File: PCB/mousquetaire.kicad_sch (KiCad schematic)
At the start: 34 parts, among them J1 Sum2, J2 Sum3, J3 Sum1, J5 SUM, J6 Mi, J7 M1, J8 M2, J9 M3, U1 TL072, U2 TL074

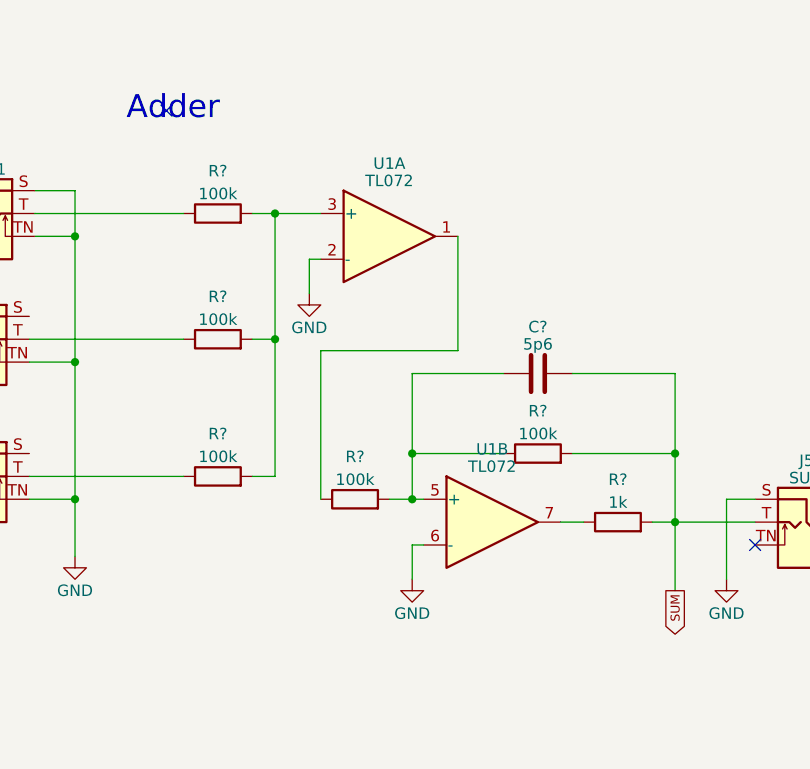
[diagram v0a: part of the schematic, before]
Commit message: :pencil2: Fix the adder circuit
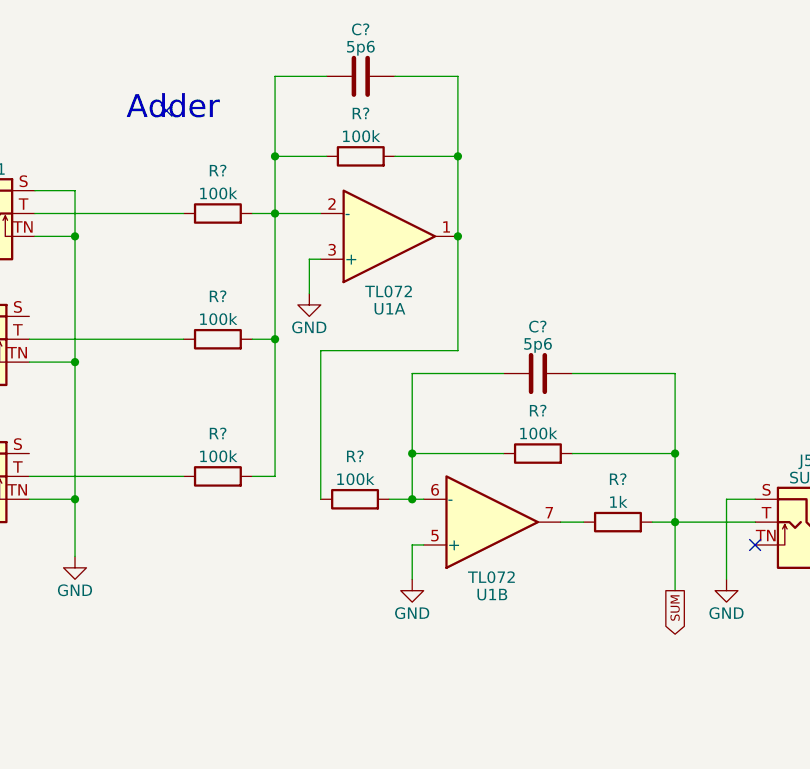
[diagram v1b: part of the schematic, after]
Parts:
- added C?: 5p6, Capacitor_THT:C_Disc_D4.3mm_W1.9mm_P5.00mm, symbol Device:C
- added R?: 100k, Resistor_THT:R_Axial_DIN0207_L6.3mm_D2.5mm_P7.62mm_Horizontal, symbol Device:R
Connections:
- net GND: now also U1.3 (+), U1.5 (+); no longer U1.2 (-), U1.6 (-)
- net at R?.2, R?.2, R?.2: now also U1.2 (-), C?.1, R?.1; no longer U1.3 (+)
- net at R?.1, U1.1: now also C?.2, R?.2
- net at C?.1, R?.1, R?.2: now also U1.6 (-); no longer U1.5 (+)

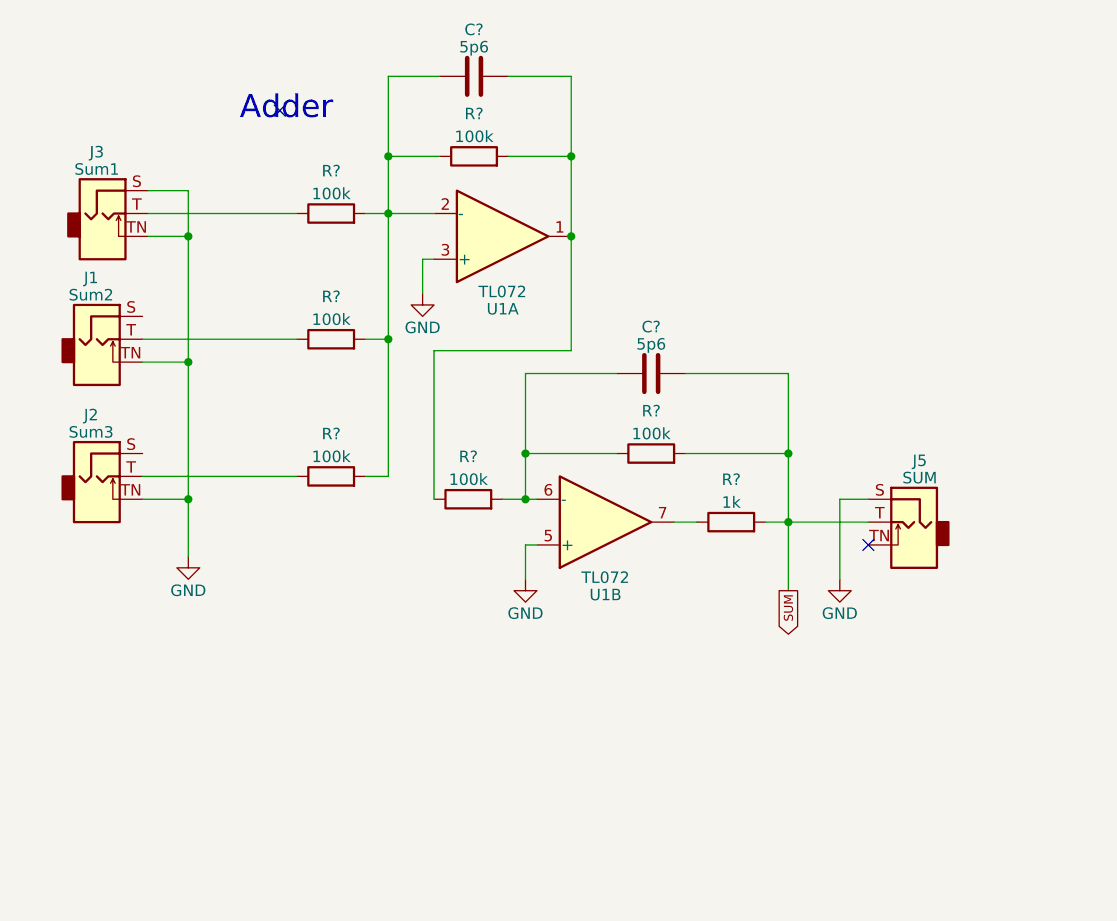
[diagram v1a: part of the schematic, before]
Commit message: :pencil2: Add missing changes for the adder fix
Somehow not everything had been committed for #2. This is the fix. :/
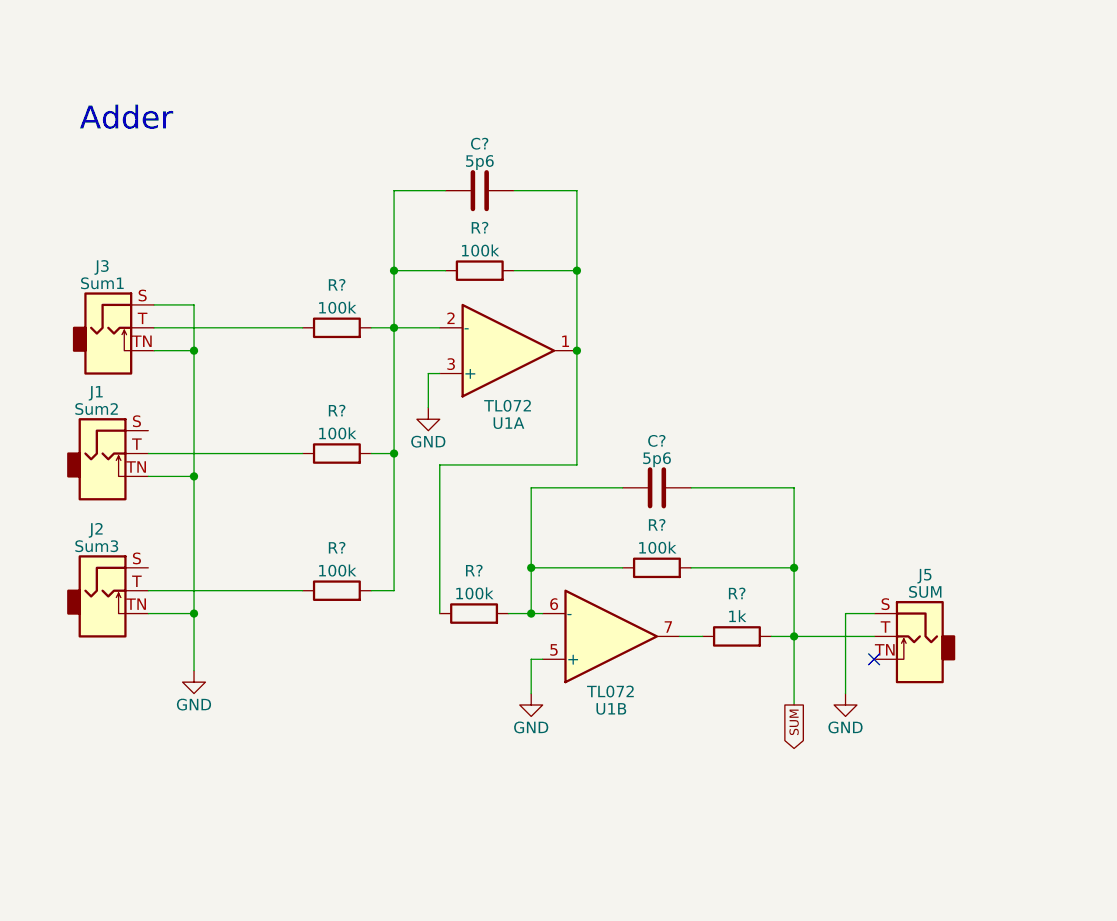
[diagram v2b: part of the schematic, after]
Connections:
- no-connect marks 5 -> 4
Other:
- moved on the sheet: C?, J1, J2, J3, J5, R?, U1A, U1B

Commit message: :art: Improvements to schematic for PCB design
Mostly interchanging components for easier routing.
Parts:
- renumbered R9 to R10, R10 to R11, R7 to R8, R8 to R9
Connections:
- net at U2.6 (-), U2.7: now also R11.1; no longer R10.1
- net at U2.8, U2.9 (-): now also R9.1; no longer R11.1
- net at U2.1, U2.2 (-): now also R10.1; no longer R9.1
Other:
- moved on the sheet: U2A, U2B, U2C
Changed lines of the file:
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@@
       (project "mousquetaire"
         (path "/6467167b-c991-4ed5-b6bb-0d17859f2985"
-          (reference "R11") (unit 1)
+          (reference "R5") (unit 1)
         )
       )
@@
       (project "mousquetaire"
         (path "/6467167b-c991-4ed5-b6bb-0d17859f2985"
-          (reference "C4") (unit 1)
+          (reference "C5") (unit 1)
         )
       )
@@
       (project "mousquetaire"
         (path "/6467167b-c991-4ed5-b6bb-0d17859f2985"
-          (reference "C9") (unit 1)
+          (reference "C10") (unit 1)
         )
       )
@@
       (project "mousquetaire"
         (path "/6467167b-c991-4ed5-b6bb-0d17859f2985"
-          (reference "C7") (unit 1)
+          (reference "C8") (unit 1)
         )
       )
@@
   (symbol (lib_id "Device:R") (at 210.82 60.325 90) (unit 1)
     (in_bom yes) (on_board yes) (dnp no) (fields_autoplaced)
-    (property "Reference" "R9" (at 210.82 55.6092 90)
+    (property "Reference" "R10" (at 210.82 55.6092 90)
       (effects (font (size 1.27 1.27)))
     )
@@
       (project "mousquetaire"
         (path "/6467167b-c991-4ed5-b6bb-0d17859f2985"
-          (reference "R9") (unit 1)
+          (reference "R10") (unit 1)
         )
       )
@@
       (project "mousquetaire"
         (path "/6467167b-c991-4ed5-b6bb-0d17859f2985"
-          (reference "C10") (unit 1)
+          (reference "C3") (unit 1)
         )
       )
@@
     )
   )
-  (symbol (lib_id "Amplifier_Operational:TL074") (at 195.58 60.325 0) (unit 2)
-    (in_bom yes) (on_board yes) (dnp no) (fields_autoplaced)
-    (property "Reference" "U2" (at 195.58 52.2351 0)
-      (effects (font (size 1.27 1.27)))
-    )
-    (property "Value" "TL074" (at 195.58 54.1561 0)
-      (effects (font (size 1.27 1.27)))
-    )
-    (property "Footprint" "Package_DIP:DIP-14_W7.62mm_Socket_LongPads" (at 194.31 57.785 0)
-      (effects (font (size 1.27 1.27)) hide)
-    )
-    (property "Datasheet" "http://www.ti.com/lit/ds/symlink/tl071.pdf" (at 196.85 55.245 0)
+  (symbol (lib_id "Amplifier_Operational:TL074") (at 195.58 78.105 0) (unit 2)
+    (in_bom yes) (on_board yes) (dnp no) (fields_autoplaced)
+    (property "Reference" "U2" (at 195.58 70.0151 0)
+      (effects (font (size 1.27 1.27)))
+    )
+    (property "Value" "TL074" (at 195.58 71.9361 0)
+      (effects (font (size 1.27 1.27)))
+    )
+    (property "Footprint" "Package_DIP:DIP-14_W7.62mm_Socket_LongPads" (at 194.31 75.565 0)
+      (effects (font (size 1.27 1.27)) hide)
+    )
+    (property "Datasheet" "http://www.ti.com/lit/ds/symlink/tl071.pdf" (at 196.85 73.025 0)
       (effects (font (size 1.27 1.27)) hide)
     )
@@
   (symbol (lib_id "Device:R") (at 210.82 78.105 90) (unit 1)
     (in_bom yes) (on_board yes) (dnp no) (fields_autoplaced)
-    (property "Reference" "R10" (at 210.82 73.3892 90)
+    (property "Reference" "R11" (at 210.82 73.3892 90)
       (effects (font (size 1.27 1.27)))
     )
@@
       (project "mousquetaire"
         (path "/6467167b-c991-4ed5-b6bb-0d17859f2985"
-          (reference "R10") (unit 1)
+          (reference "R11") (unit 1)
         )
       )
@@
       (project "mousquetaire"
         (path "/6467167b-c991-4ed5-b6bb-0d17859f2985"
-          (reference "C6") (unit 1)
+          (reference "C7") (unit 1)
         )
       )
@@
       (project "mousquetaire"
         (path "/6467167b-c991-4ed5-b6bb-0d17859f2985"
-          (reference "R6") (unit 1)
-        )
-      )
-    )
-  )
-  (symbol (lib_id "Amplifier_Operational:TL074") (at 194.31 38.735 0) (unit 1)
-    (in_bom yes) (on_board yes) (dnp no) (fields_autoplaced)
-    (property "Reference" "U2" (at 194.31 30.6451 0)
-      (effects (font (size 1.27 1.27)))
-    )
-    (property "Value" "TL074" (at 194.31 32.5661 0)
-      (effects (font (size 1.27 1.27)))
-    )
-    (property "Footprint" "Package_DIP:DIP-14_W7.62mm_Socket_LongPads" (at 193.04 36.195 0)
-      (effects (font (size 1.27 1.27)) hide)
-    )
-    (property "Datasheet" "http://www.ti.com/lit/ds/symlink/tl071.pdf" (at 195.58 33.655 0)
+          (reference "R7") (unit 1)
+        )
+      )
+    )
+  )
+  (symbol (lib_id "Amplifier_Operational:TL074") (at 195.58 60.325 0) (unit 1)
+    (in_bom yes) (on_board yes) (dnp no) (fields_autoplaced)
+    (property "Reference" "U2" (at 195.58 52.2351 0)
+      (effects (font (size 1.27 1.27)))
+    )
+    (property "Value" "TL074" (at 195.58 54.1561 0)
+      (effects (font (size 1.27 1.27)))
+    )
+    (property "Footprint" "Package_DIP:DIP-14_W7.62mm_Socket_LongPads" (at 194.31 57.785 0)
+      (effects (font (size 1.27 1.27)) hide)
+    )
+    (property "Datasheet" "http://www.ti.com/lit/ds/symlink/tl071.pdf" (at 196.85 55.245 0)
       (effects (font (size 1.27 1.27)) hide)
     )
@@
       (project "mousquetaire"
         (path "/6467167b-c991-4ed5-b6bb-0d17859f2985"
-          (reference "R5") (unit 1)
+          (reference "R6") (unit 1)
         )
       )
@@
       (project "mousquetaire"
         (path "/6467167b-c991-4ed5-b6bb-0d17859f2985"
-          (reference "C3") (unit 1)
+          (reference "C4") (unit 1)
         )
       )
@@
       (project "mousquetaire"
         (path "/6467167b-c991-4ed5-b6bb-0d17859f2985"
-          (reference "C8") (unit 1)
+          (reference "C9") (unit 1)
         )
       )
@@
   (symbol (lib_id "Device:R") (at 175.26 36.195 90) (unit 1)
     (in_bom yes) (on_board yes) (dnp no) (fields_autoplaced)
-    (property "Reference" "R7" (at 175.26 31.4792 90)
+    (property "Reference" "R8" (at 175.26 31.4792 90)
       (effects (font (size 1.27 1.27)))
     )
@@
       (project "mousquetaire"
         (path "/6467167b-c991-4ed5-b6bb-0d17859f2985"
-          (reference "R7") (unit 1)
+          (reference "R8") (unit 1)
         )
       )
@@
   (symbol (lib_id "Device:R") (at 210.82 38.735 90) (unit 1)
     (in_bom yes) (on_board yes) (dnp no) (fields_autoplaced)
-    (property "Reference" "R8" (at 210.82 34.0192 90)
+    (property "Reference" "R9" (at 210.82 34.0192 90)
       (effects (font (size 1.27 1.27)))
     )
@@
       (project "mousquetaire"
         (path "/6467167b-c991-4ed5-b6bb-0d17859f2985"
-          (reference "R8") (unit 1)
+          (reference "R9") (unit 1)
         )
       )
@@
       (project "mousquetaire"
         (path "/6467167b-c991-4ed5-b6bb-0d17859f2985"
-          (reference "C5") (unit 1)
-        )
-      )
-    )
-  )
-  (symbol (lib_id "Amplifier_Operational:TL074") (at 195.58 78.105 0) (unit 3)
-    (in_bom yes) (on_board yes) (dnp no) (fields_autoplaced)
-    (property "Reference" "U2" (at 195.58 70.0151 0)
-      (effects (font (size 1.27 1.27)))
-    )
-    (property "Value" "TL074" (at 195.58 71.9361 0)
-      (effects (font (size 1.27 1.27)))
-    )
-    (property "Footprint" "Package_DIP:DIP-14_W7.62mm_Socket_LongPads" (at 194.31 75.565 0)
-      (effects (font (size 1.27 1.27)) hide)
-    )
-    (property "Datasheet" "http://www.ti.com/lit/ds/symlink/tl071.pdf" (at 196.85 73.025 0)
-      (effects (font (size 1.27 1.27)) hide)
-    )
+          (reference "C6") (unit 1)
+        )
+      )
+    )
+  )
+  (symbol (lib_id "Amplifier_Operational:TL074") (at 194.31 38.735 0) (unit 3)
+    (in_bom yes) (on_board yes) (dnp no) (fields_autoplaced)
+    (property "Reference" "U2" (at 194.31 30.6451 0)
+      (effects (font (size 1.27 1.27)))
+    )
+    (property "Value" "TL074" (at 194.31 32.5661 0)
+      (effects (font (size 1.27 1.27)))
+    )
+    (property "Footprint" "Package_DIP:DIP-14_W7.62mm_Socket_LongPads" (at 193.04 36.195 0)
+      (effects (font (size 1.27 1.27)) hide)
+    )
+    (property "Datasheet" "http://www.ti.com/lit/ds/symlink/tl071.pdf" (at 195.58 33.655 0)
+      (effects (font (size 1.27 1.27)) hide)
+    )

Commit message: :hammer: Change power connector to vertical footprint
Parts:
- J?: footprint Connector_PinHeader_2.54mm:PinHeader_2x05_P2.54mm_Horizontal -> Connector_PinHeader_2.54mm:PinHeader_2x05_P2.54mm_Vertical
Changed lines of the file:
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@@
       (effects (font (size 1.27 1.27)))
     )
-    (property "Footprint" "Connector_PinHeader_2.54mm:PinHeader_2x05_P2.54mm_Horizontal" (at 30.48 176.53 0)
+    (property "Footprint" "Connector_PinHeader_2.54mm:PinHeader_2x05_P2.54mm_Vertical" (at 30.48 176.53 0)
       (effects (font (size 1.27 1.27)) hide)
     )
